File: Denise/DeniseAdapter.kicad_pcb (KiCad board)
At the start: 2 copper layers, 29.2 x 63.5 mm, 7 parts, among them J1 Conn_01x01, J2 Conn_01x01, J3 Conn_01x01, J4 Conn_01x01, U1 Denise, U2 Denise_PLCC

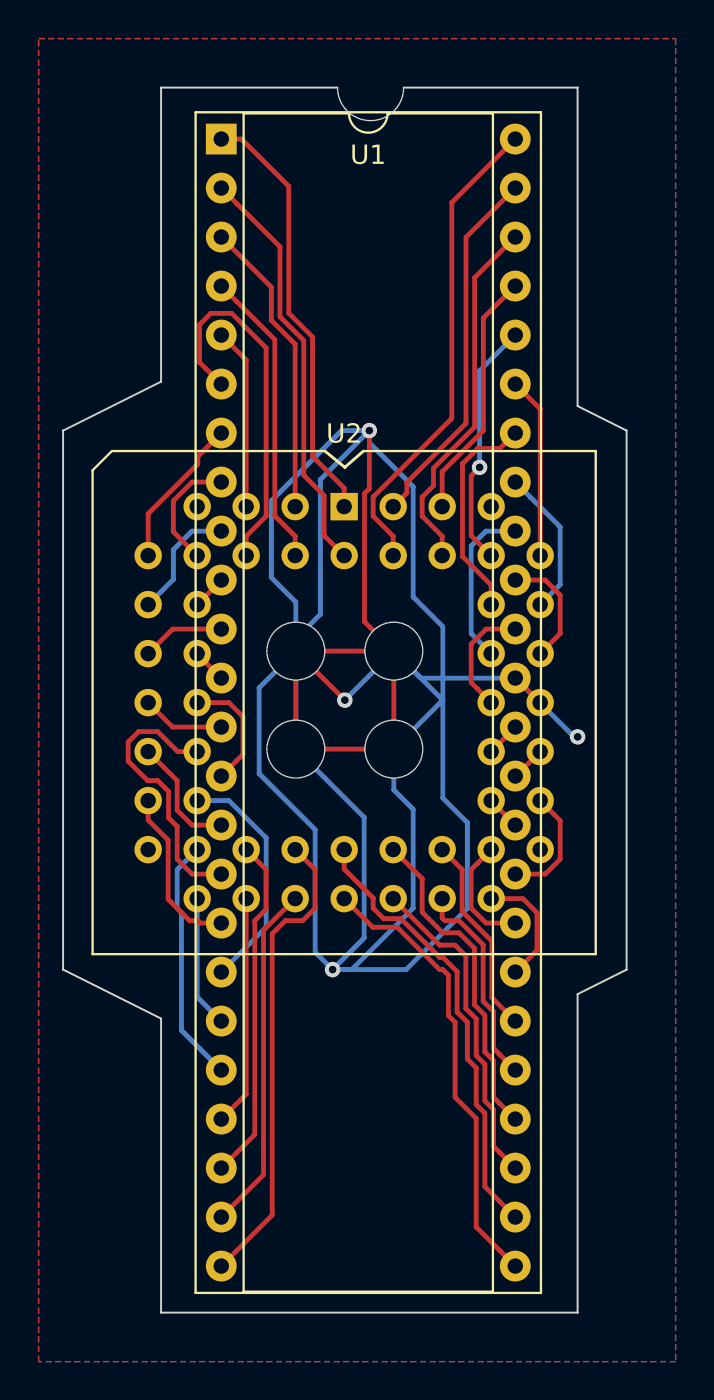
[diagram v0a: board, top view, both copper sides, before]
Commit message: nicer board outline for Denise adapter
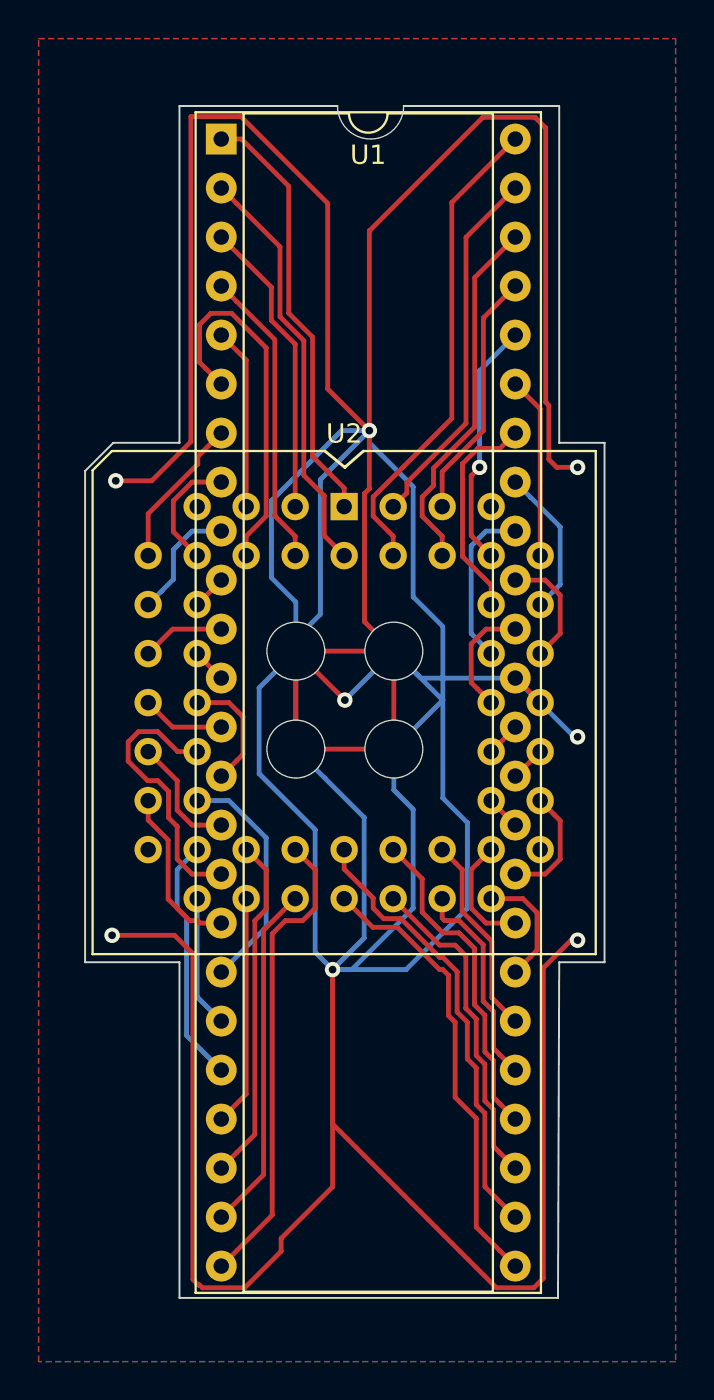
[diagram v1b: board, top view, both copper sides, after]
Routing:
- net /VSS: track 174.8 -> 342.9 mm, vias 4 -> 8
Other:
- board size 29.2 x 63.5 mm -> 26.9 x 61.8 mm
